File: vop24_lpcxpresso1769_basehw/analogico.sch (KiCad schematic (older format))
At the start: 8 parts

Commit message: Esquematico Comunicacion: falta agregar USB, BLE y UART
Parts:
- added U?: LM358, symbol Amplifier_Operational:LM358
- R? (x5), RTD?: symbol R_Small -> Device:R_Small
- U? (x2): symbol LM358 -> Amplifier_Operational:LM358
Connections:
- wire segments 40 -> 41

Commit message: Primera versión esquematico sin revisar
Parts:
- gave numbers to parts that had none: 8
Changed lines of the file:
@@
 $EndDescr
 $Comp
-L Amplifier_Operational:LM358 U?
+L Amplifier_Operational:LM358 U3
 U 1 1 5B3D221E
 P 4600 2850
-F 0 "U?" H 4600 3050 50  0000 L CNN
+F 0 "U3" H 4600 3050 50  0000 L CNN
 F 1 "LM358" H 4600 2650 50  0000 L CNN
 F 2 "" H 4600 2850 50  0001 C CNN
@@
 $EndComp
 $Comp
-L Device:R_Small R?
+L Device:R_Small R2
 U 1 1 5B3D2225
 P 3600 2650
-F 0 "R?" H 3630 2670 50  0000 L CNN
+F 0 "R2" H 3630 2670 50  0000 L CNN
 F 1 "R_Small" H 3630 2610 50  0000 L CNN
 F 2 "" H 3600 2650 50  0001 C CNN
@@
 $EndComp
 $Comp
-L Device:R_Small R?
+L Device:R_Small R3
 U 1 1 5B3D222C
 P 3600 3200
-F 0 "R?" H 3630 3220 50  0000 L CNN
+F 0 "R3" H 3630 3220 50  0000 L CNN
 F 1 "R_Small" H 3630 3160 50  0000 L CNN
 F 2 "" H 3600 3200 50  0001 C CNN
@@
 AGND
 $Comp
-L Amplifier_Operational:LM358 U?
+L Amplifier_Operational:LM358 U2
 U 1 1 5B3D2D53
 P 4450 5250
-F 0 "U?" H 4450 5450 50  0000 L CNN
+F 0 "U2" H 4450 5450 50  0000 L CNN
 F 1 "LM358" H 4450 5050 50  0000 L CNN
 F 2 "" H 4450 5250 50  0001 C CNN
@@
 $EndComp
 $Comp
-L Device:R_Small R?
+L Device:R_Small R1
 U 1 1 5B3D2D5A
 P 3500 4850
-F 0 "R?" H 3530 4870 50  0000 L CNN
+F 0 "R1" H 3530 4870 50  0000 L CNN
 F 1 "R_Small" H 3530 4810 50  0000 L CNN
 F 2 "" H 3500 4850 50  0001 C CNN
@@
 $EndComp
 $Comp
-L Device:R_Small RTD?
+L Device:R_Small RTD1
 U 1 1 5B3D2D61
 P 3500 5200
-F 0 "RTD?" H 3530 5220 50  0000 L CNN
+F 0 "RTD1" H 3530 5220 50  0000 L CNN
 F 1 "R_Small" H 3530 5160 50  0000 L CNN
 F 2 "" H 3500 5200 50  0001 C CNN
@@
 $EndComp
 $Comp
-L Device:R_Small R?
+L Device:R_Small R4
 U 1 1 5B3D2D68
 P 3700 5500
-F 0 "R?" H 3730 5520 50  0000 L CNN
+F 0 "R4" H 3730 5520 50  0000 L CNN
 F 1 "R_Small" H 3730 5460 50  0000 L CNN
 F 2 "" H 3700 5500 50  0001 C CNN
@@
 $EndComp
 $Comp
-L Device:R_Small R?
+L Device:R_Small R5
 U 1 1 5B3D2D6F
 P 4300 5850
-F 0 "R?" H 4330 5870 50  0000 L CNN
+F 0 "R5" H 4330 5870 50  0000 L CNN
 F 1 "R_Small" H 4330 5810 50  0000 L CNN
 F 2 "" H 4300 5850 50  0001 C CNN
@@
 	5450 2850 6150 2850
 $Comp
-L Amplifier_Operational:LM358 U?
+L Amplifier_Operational:LM358 U2
 U 3 1 5B65ECB1
 P 8250 2700
-F 0 "U?" H 8250 2900 50  0000 L CNN
+F 0 "U2" H 8250 2900 50  0000 L CNN
 F 1 "LM358" H 8250 2500 50  0000 L CNN
 F 2 "" H 8250 2700 50  0001 C CNN

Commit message: Algunas correcciones sobre el esquemático. Falta terminar de revisar algunos conflictos del DRC
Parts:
- renumbered R1 to R201, R2 to R202, R3 to R203, R4 to R204, R5 to R205, RTD1 to RTD201, U2 to U201, U3 to U202
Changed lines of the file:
@@
 $Descr A4 11693 8268
 encoding utf-8
-Sheet 3 5
+Sheet 2 5
 Title "Entradas analogicas"
 Date "2018-07-04"
@@
 $EndDescr
 $Comp
-L Amplifier_Operational:LM358 U3
+L Amplifier_Operational:LM358 U202
 U 1 1 5B3D221E
 P 4600 2850
-F 0 "U3" H 4600 3050 50  0000 L CNN
+F 0 "U202" H 4600 3050 50  0000 L CNN
 F 1 "LM358" H 4600 2650 50  0000 L CNN
 F 2 "" H 4600 2850 50  0001 C CNN
@@
 $EndComp
 $Comp
-L Device:R_Small R2
+L Device:R_Small R202
 U 1 1 5B3D2225
 P 3600 2650
-F 0 "R2" H 3630 2670 50  0000 L CNN
+F 0 "R202" H 3630 2670 50  0000 L CNN
 F 1 "R_Small" H 3630 2610 50  0000 L CNN
 F 2 "" H 3600 2650 50  0001 C CNN
@@
 $EndComp
 $Comp
-L Device:R_Small R3
+L Device:R_Small R203
 U 1 1 5B3D222C
 P 3600 3200
-F 0 "R3" H 3630 3220 50  0000 L CNN
+F 0 "R203" H 3630 3220 50  0000 L CNN
 F 1 "R_Small" H 3630 3160 50  0000 L CNN
 F 2 "" H 3600 3200 50  0001 C CNN
@@
 AGND
 $Comp
-L Amplifier_Operational:LM358 U2
+L Amplifier_Operational:LM358 U201
 U 1 1 5B3D2D53
 P 4450 5250
-F 0 "U2" H 4450 5450 50  0000 L CNN
+F 0 "U201" H 4450 5450 50  0000 L CNN
 F 1 "LM358" H 4450 5050 50  0000 L CNN
 F 2 "" H 4450 5250 50  0001 C CNN
@@
 $EndComp
 $Comp
-L Device:R_Small R1
+L Device:R_Small R201
 U 1 1 5B3D2D5A
 P 3500 4850
-F 0 "R1" H 3530 4870 50  0000 L CNN
+F 0 "R201" H 3530 4870 50  0000 L CNN
 F 1 "R_Small" H 3530 4810 50  0000 L CNN
 F 2 "" H 3500 4850 50  0001 C CNN
@@
 $EndComp
 $Comp
-L Device:R_Small RTD1
+L Device:R_Small RTD201
 U 1 1 5B3D2D61
 P 3500 5200
-F 0 "RTD1" H 3530 5220 50  0000 L CNN
+F 0 "RTD201" H 3530 5220 50  0000 L CNN
 F 1 "R_Small" H 3530 5160 50  0000 L CNN
 F 2 "" H 3500 5200 50  0001 C CNN
@@
 $EndComp
 $Comp
-L Device:R_Small R4
+L Device:R_Small R204
 U 1 1 5B3D2D68
 P 3700 5500
-F 0 "R4" H 3730 5520 50  0000 L CNN
+F 0 "R204" H 3730 5520 50  0000 L CNN
 F 1 "R_Small" H 3730 5460 50  0000 L CNN
 F 2 "" H 3700 5500 50  0001 C CNN
@@
 $EndComp
 $Comp
-L Device:R_Small R5
+L Device:R_Small R205
 U 1 1 5B3D2D6F
 P 4300 5850
-F 0 "R5" H 4330 5870 50  0000 L CNN
+F 0 "R205" H 4330 5870 50  0000 L CNN
 F 1 "R_Small" H 4330 5810 50  0000 L CNN
 F 2 "" H 4300 5850 50  0001 C CNN
@@
 	5450 2850 6150 2850
 $Comp
-L Amplifier_Operational:LM358 U2
+L Amplifier_Operational:LM358 U201
 U 3 1 5B65ECB1
 P 8250 2700
-F 0 "U2" H 8250 2900 50  0000 L CNN
+F 0 "U201" H 8250 2900 50  0000 L CNN
 F 1 "LM358" H 8250 2500 50  0000 L CNN
 F 2 "" H 8250 2700 50  0001 C CNN

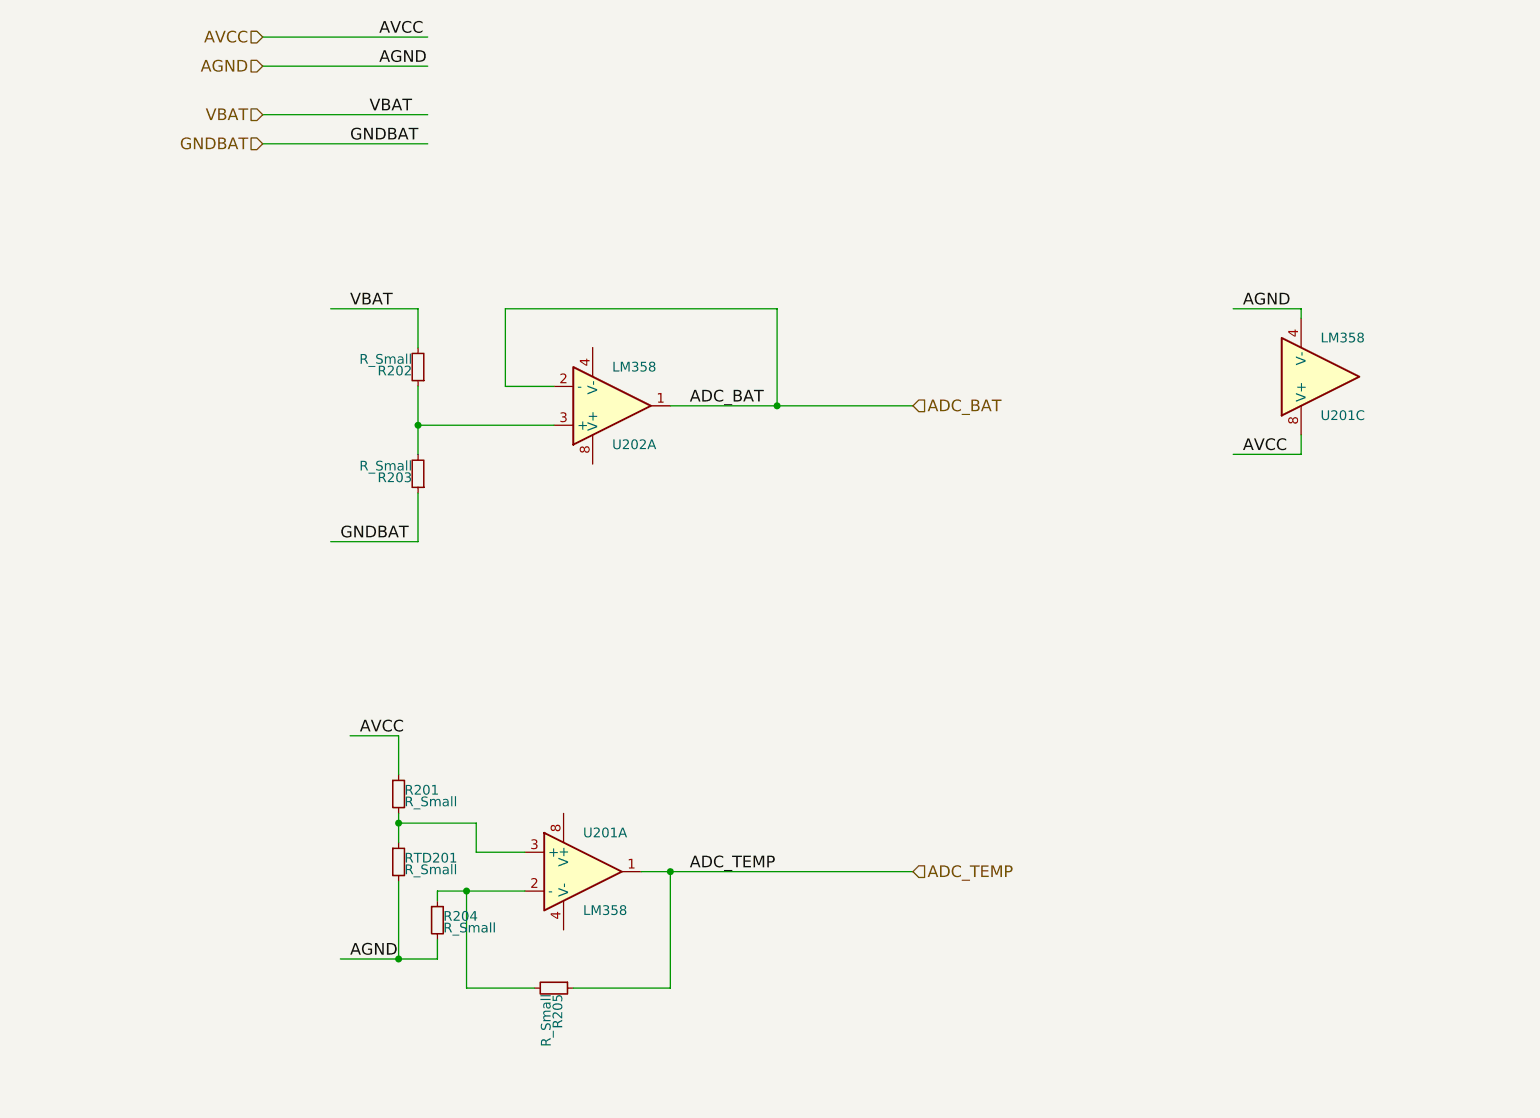
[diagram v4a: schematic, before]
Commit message: Correcciones de esquemático:    - resueltos todos los conflictos de DRC    - cambio de circutio de medicion de temp    - ordenados todas las etiquetas y valores
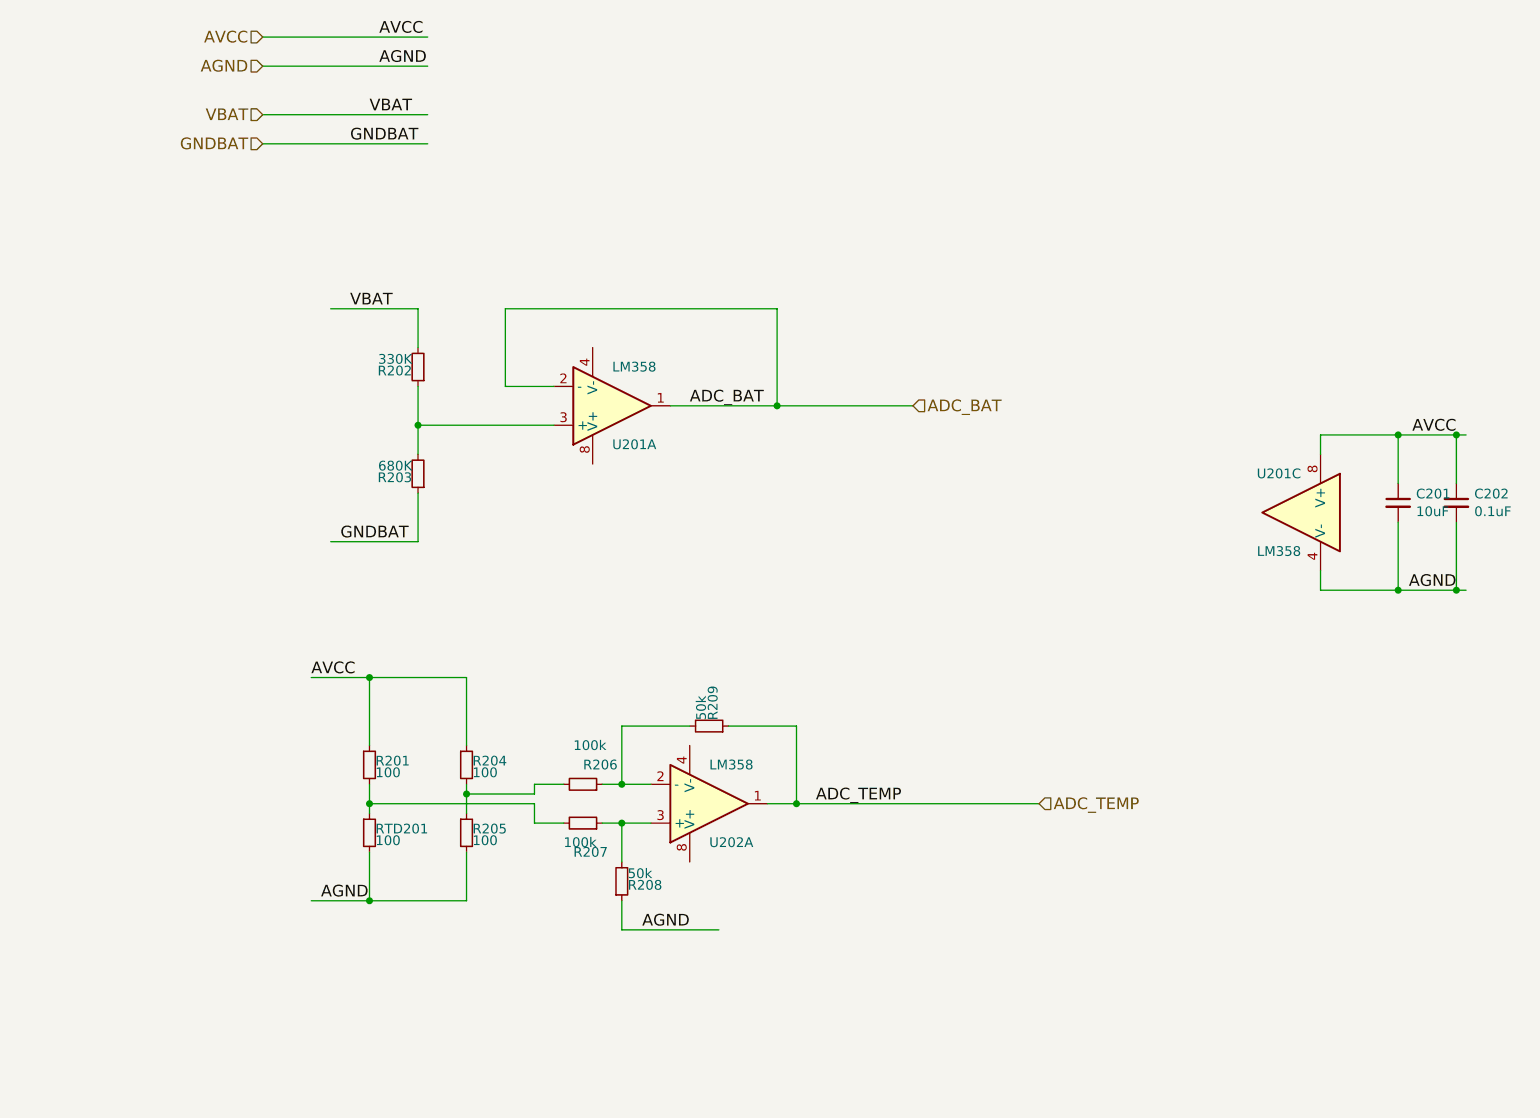
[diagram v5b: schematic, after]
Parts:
- added C201: 10uF, symbol Device:C_Small
- added C202: 0.1uF, symbol Device:C_Small
- added R205: 100, symbol Device:R_Small
- added R206, R207: 100k, symbol Device:R_Small
- added R208: 50k, symbol Device:R_Small
- R201, R204, RTD201: value R_Small -> 100
- R202: value R_Small -> 330K
- R203: value R_Small -> 680K
- R209: renamed from R205; value R_Small -> 50k
- renumbered U202 to U201, U201 to U202
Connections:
- wire segments 41 -> 60
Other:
- moved on the sheet: R209, U201C, U202A

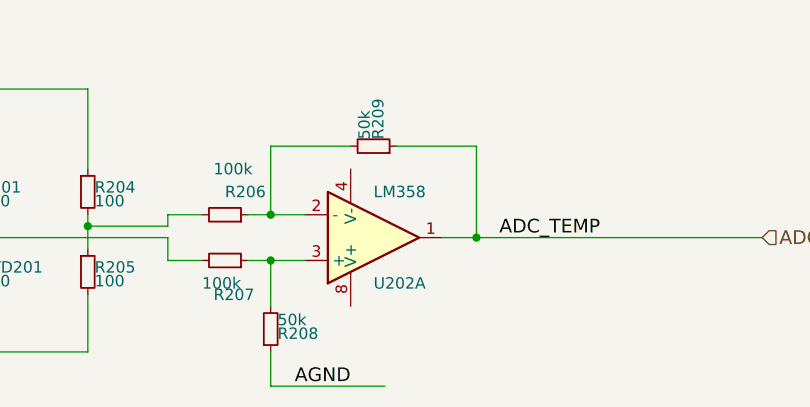
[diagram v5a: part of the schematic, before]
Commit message: Se agregaron la mayoría de los footprints de los ICs
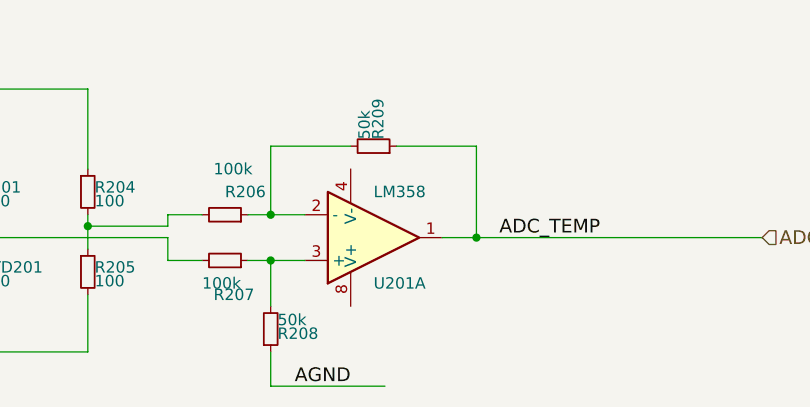
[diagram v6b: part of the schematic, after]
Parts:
- U201: footprint (none) -> Package_SO:SO-8_5.3x6.2mm_P1.27mm
- U201: renamed from U202; footprint (none) -> Package_SO:SOIC-8_3.9x4.9mm_P1.27mm
- U201: footprint (none) -> Package_SO:SOIC-8_3.9x4.9mm_P1.27mm
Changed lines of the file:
@@
 F 0 "U201" H 4600 3050 50  0000 L CNN
 F 1 "LM358" H 4600 2650 50  0000 L CNN
-F 2 "" H 4600 2850 50  0001 C CNN
+F 2 "Package_SO:SO-8_5.3x6.2mm_P1.27mm" H 4600 2850 50  0001 C CNN
 F 3 "" H 4600 2850 50  0001 C CNN
 	1    4600 2850
@@
 AGND
 $Comp
-L Amplifier_Operational:LM358 U202
+L Amplifier_Operational:LM358 U201
 U 1 1 5B3D2D53
 P 5100 4900
-F 0 "U202" H 5100 5100 50  0000 L CNN
+F 0 "U201" H 5100 5100 50  0000 L CNN
 F 1 "LM358" H 5100 4700 50  0000 L CNN
-F 2 "" H 5100 4900 50  0001 C CNN
+F 2 "Package_SO:SOIC-8_3.9x4.9mm_P1.27mm" H 5100 4900 50  0001 C CNN
 F 3 "" H 5100 4900 50  0001 C CNN
 	1    5100 4900
@@
 F 0 "U201" H 8150 3600 50  0000 L CNN
 F 1 "LM358" H 8150 3200 50  0000 L CNN
-F 2 "" H 8150 3400 50  0001 C CNN
+F 2 "Package_SO:SOIC-8_3.9x4.9mm_P1.27mm" H 8150 3400 50  0001 C CNN
 F 3 "" H 8150 3400 50  0001 C CNN
 	3    8150 3400

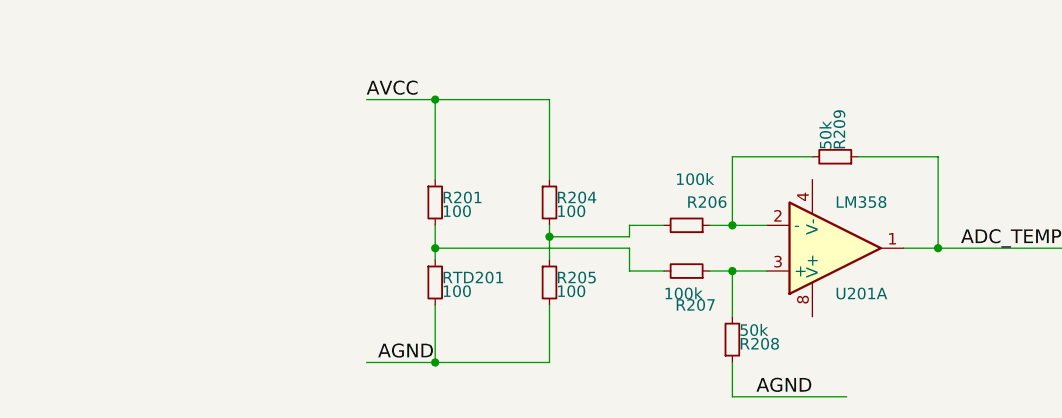
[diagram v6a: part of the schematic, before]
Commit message: Finalizada asociación de todos los footprints. Ver librerías froux-kicad
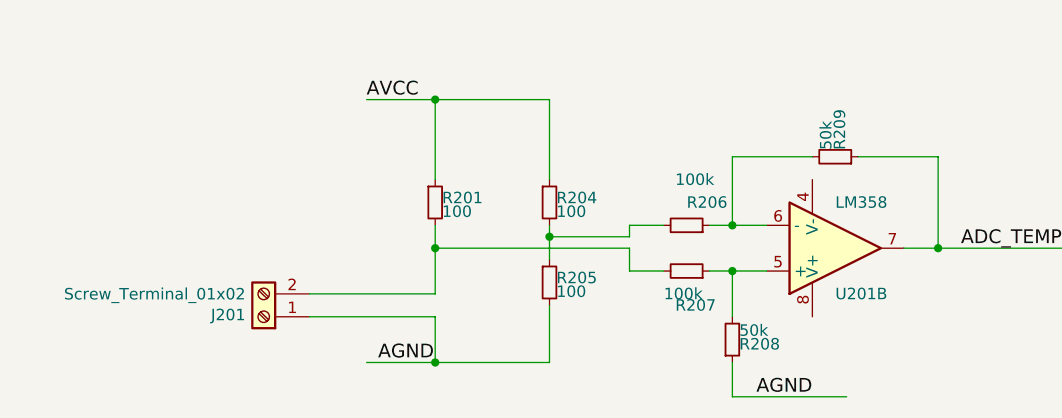
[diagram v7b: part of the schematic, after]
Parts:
- removed RTD201: 100, symbol Device:R_Small
- added J201: Screw_Terminal_01x02, TerminalBlock:TerminalBlock_bornier-2_P5.08mm, symbol Connector:Screw_Terminal_01x02
- C201, C202: footprint (none) -> Capacitor_SMD:C_0805_2012Metric_Pad1.15x1.40mm_HandSolder
- R201, R202, R203, R204, R205, R206, R207, R208, R209: footprint (none) -> Resistor_SMD:R_0805_2012Metric_Pad1.15x1.40mm_HandSolder
- U201: footprint Package_SO:SOIC-8_3.9x4.9mm_P1.27mm -> Package_SO:SO-8_5.3x6.2mm_P1.27mm
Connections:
- wire segments 60 -> 62
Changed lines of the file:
@@
 F 0 "R202" H 3630 2670 50  0000 L CNN
 F 1 "330K" H 3630 2610 50  0000 L CNN
-F 2 "" H 3600 2650 50  0001 C CNN
+F 2 "Resistor_SMD:R_0805_2012Metric_Pad1.15x1.40mm_HandSolder" H 3600 2650 50  0001 C CNN
 F 3 "" H 3600 2650 50  0001 C CNN
 	1    3600 2650
@@
 F 0 "R203" H 3630 3220 50  0000 L CNN
 F 1 "680K" H 3630 3160 50  0000 L CNN
-F 2 "" H 3600 3200 50  0001 C CNN
+F 2 "Resistor_SMD:R_0805_2012Metric_Pad1.15x1.40mm_HandSolder" H 3600 3200 50  0001 C CNN
 F 3 "" H 3600 3200 50  0001 C CNN
 	1    3600 3200
@@
 $Comp
 L Amplifier_Operational:LM358 U201
-U 1 1 5B3D2D53
+U 2 1 5B3D2D53
 P 5100 4900
 F 0 "U201" H 5100 5100 50  0000 L CNN
 F 1 "LM358" H 5100 4700 50  0000 L CNN
-F 2 "Package_SO:SOIC-8_3.9x4.9mm_P1.27mm" H 5100 4900 50  0001 C CNN
+F 2 "Package_SO:SO-8_5.3x6.2mm_P1.27mm" H 5100 4900 50  0001 C CNN
 F 3 "" H 5100 4900 50  0001 C CNN
-	1    5100 4900
+	2    5100 4900
 	1    0    0    1
 $EndComp
@@
 F 0 "R209" H 5130 4520 50  0000 L CNN
 F 1 "50k" H 5130 4460 50  0000 L CNN
-F 2 "" H 5100 4500 50  0001 C CNN
+F 2 "Resistor_SMD:R_0805_2012Metric_Pad1.15x1.40mm_HandSolder" H 5100 4500 50  0001 C CNN
 F 3 "" H 5100 4500 50  0001 C CNN
 	1    5100 4500
@@
 F 0 "U201" H 8150 3600 50  0000 L CNN
 F 1 "LM358" H 8150 3200 50  0000 L CNN
-F 2 "Package_SO:SOIC-8_3.9x4.9mm_P1.27mm" H 8150 3400 50  0001 C CNN
+F 2 "Package_SO:SO-8_5.3x6.2mm_P1.27mm" H 8150 3400 50  0001 C CNN
 F 3 "" H 8150 3400 50  0001 C CNN
 	3    8150 3400
@@
 F 0 "C201" H 8742 3396 50  0000 L CNN
 F 1 "10uF" H 8742 3305 50  0000 L CNN
-F 2 "" H 8650 3350 50  0001 C CNN
+F 2 "Capacitor_SMD:C_0805_2012Metric_Pad1.15x1.40mm_HandSolder" H 8650 3350 50  0001 C CNN
 F 3 "~" H 8650 3350 50  0001 C CNN
 	1    8650 3350
@@
 F 0 "C202" H 9042 3396 50  0000 L CNN
 F 1 "0.1uF" H 9042 3305 50  0000 L CNN
-F 2 "" H 8950 3350 50  0001 C CNN
+F 2 "Capacitor_SMD:C_0805_2012Metric_Pad1.15x1.40mm_HandSolder" H 8950 3350 50  0001 C CNN
 F 3 "~" H 8950 3350 50  0001 C CNN
 	1    8950 3350
@@
 Wire Wire Line
 	8950 3800 9000 3800
-$Comp
-L Device:R_Small RTD201
-U 1 1 5BE93D58
-P 3350 5050
-F 0 "RTD201" H 3380 5070 50  0000 L CNN
-F 1 "100" H 3380 5010 50  0000 L CNN
-F 2 "" H 3350 5050 50  0001 C CNN
-F 3 "" H 3350 5050 50  0001 C CNN
-	1    3350 5050
-	1    0    0    -1
-$EndComp
 $Comp
 L Device:R_Small R201
@@
 F 0 "R201" H 3380 4720 50  0000 L CNN
 F 1 "100" H 3380 4660 50  0000 L CNN
-F 2 "" H 3350 4700 50  0001 C CNN
+F 2 "Resistor_SMD:R_0805_2012Metric_Pad1.15x1.40mm_HandSolder" H 3350 4700 50  0001 C CNN
 F 3 "" H 3350 4700 50  0001 C CNN
 	1    3350 4700
@@
 F 0 "R205" H 3880 5070 50  0000 L CNN
 F 1 "100" H 3880 5010 50  0000 L CNN
-F 2 "" H 3850 5050 50  0001 C CNN
+F 2 "Resistor_SMD:R_0805_2012Metric_Pad1.15x1.40mm_HandSolder" H 3850 5050 50  0001 C CNN
 F 3 "" H 3850 5050 50  0001 C CNN
 	1    3850 5050
@@
 F 0 "R204" H 3880 4720 50  0000 L CNN
 F 1 "100" H 3880 4660 50  0000 L CNN
-F 2 "" H 3850 4700 50  0001 C CNN
+F 2 "Resistor_SMD:R_0805_2012Metric_Pad1.15x1.40mm_HandSolder" H 3850 4700 50  0001 C CNN
 F 3 "" H 3850 4700 50  0001 C CNN
 	1    3850 4700
@@
 Connection ~ 3350 4250
 Wire Wire Line
-	3350 4950 3350 4900
-Wire Wire Line
 	3850 4800 3850 4850
-Wire Wire Line
-	3350 5150 3350 5400
 Wire Wire Line
 	3350 5400 3050 5400
@@
 F 0 "R206" V 4550 4800 50  0000 L CNN
 F 1 "100k" V 4650 4750 50  0000 L CNN
-F 2 "" H 4450 4800 50  0001 C CNN
+F 2 "Resistor_SMD:R_0805_2012Metric_Pad1.15x1.40mm_HandSolder" H 4450 4800 50  0001 C CNN
 F 3 "" H 4450 4800 50  0001 C CNN
 	1    4450 4800
@@
 F 0 "R207" V 4300 4950 50  0000 L CNN
 F 1 "100k" V 4350 4900 50  0000 L CNN
-F 2 "" H 4450 5000 50  0001 C CNN
+F 2 "Resistor_SMD:R_0805_2012Metric_Pad1.15x1.40mm_HandSolder" H 4450 5000 50  0001 C CNN
 F 3 "" H 4450 5000 50  0001 C CNN
 	1    4450 5000
@@
 F 0 "R208" H 4680 5320 50  0000 L CNN
 F 1 "50k" H 4680 5260 50  0000 L CNN
-F 2 "" H 4650 5300 50  0001 C CNN
+F 2 "Resistor_SMD:R_0805_2012Metric_Pad1.15x1.40mm_HandSolder" H 4650 5300 50  0001 C CNN
 F 3 "" H 4650 5300 50  0001 C CNN
 	1    4650 5300
@@
 Wire Wire Line
 	3850 4850 3850 4950
+Wire Wire Line
+	2800 5200 3350 5200
+Wire Wire Line
+	3350 5200 3350 5400
+Wire Wire Line
+	2800 5100 3350 5100
+Wire Wire Line
+	3350 4900 3350 5100
+$Comp
+L Connector:Screw_Terminal_01x02 J?
+U 1 1 5BDCF4D0
+P 2600 5200
+AR Path="/5B9DAB38/5BDCF4D0" Ref="J?"  Part="1"
+AR Path="/5B3D187B/5BDCF4D0" Ref="J201"  Part="1"
+F 0 "J201" H 2680 5192 50  0000 L CNN
+F 1 "Screw_Terminal_01x02" H 2680 5101 50  0000 L CNN
+F 2 "TerminalBlock:TerminalBlock_bornier-2_P5.08mm" H 2600 5200 50  0001 C CNN
+F 3 "~" H 2600 5200 50  0001 C CNN
+	1    2600 5200
+	-1   0    0    1
+$EndComp
 $EndSCHEMATC
